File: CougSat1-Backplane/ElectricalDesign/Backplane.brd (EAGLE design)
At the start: 82 x 93 mm, 17 parts, among them J1 CougSat Socket, J10 CougSat Socket, J2 CougSat Socket, J3 CougSat Socket, J4 CougSat Socket, J5 Separation Switch, J6 Separation Switch, J7 CougSat Socket, J8 CougSat Socket, J9 CougSat Socket

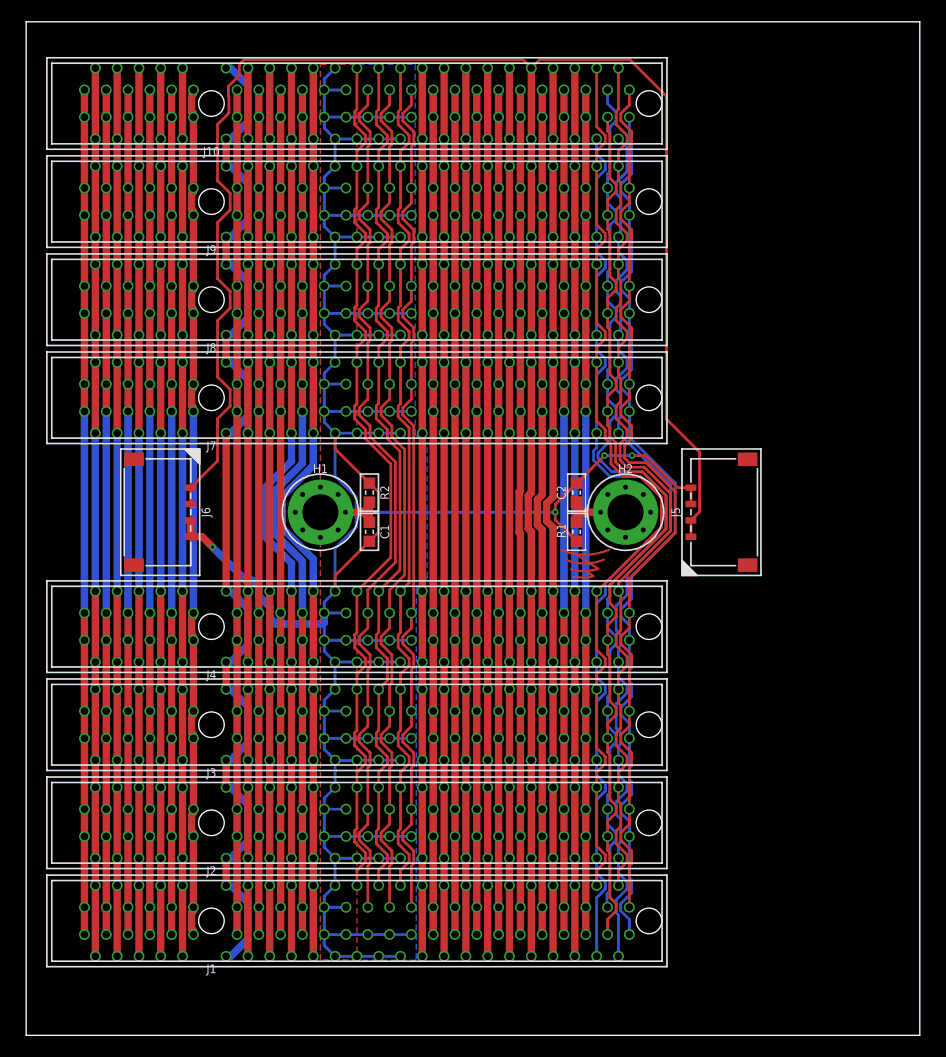
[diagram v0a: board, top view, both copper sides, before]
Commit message: Placed jacks
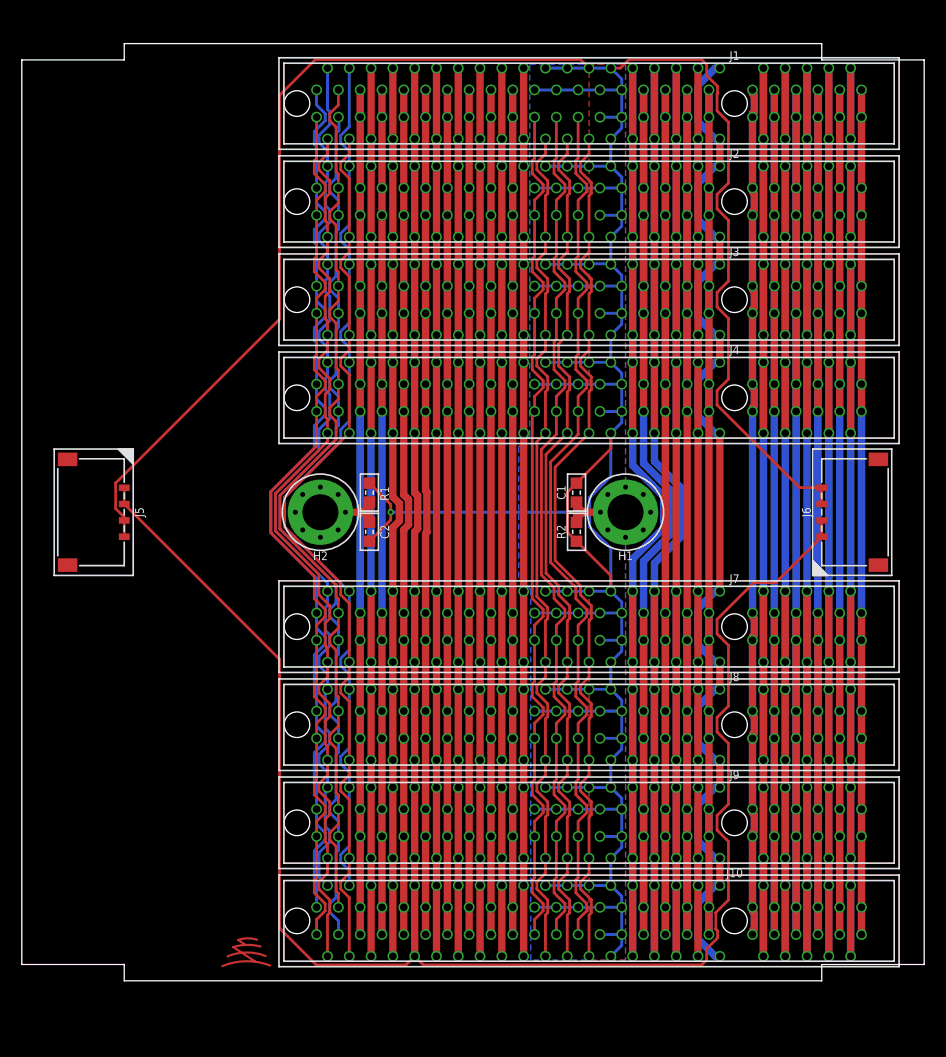
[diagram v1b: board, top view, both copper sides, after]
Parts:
- moved J1 89.0 mm to (24.0, 37.5), turned to 180 degrees
- moved J10 89.0 mm to (24.0, -37.5), turned to 180 degrees
- moved J2 74.5 mm to (24.0, 28.5), turned to 180 degrees
- moved J9 74.5 mm to (24.0, -28.5), turned to 180 degrees
- moved J3 61.8 mm to (24.0, 19.5), turned to 180 degrees
- moved J8 61.8 mm to (24.0, -19.5), turned to 180 degrees
- moved J6 57.9 mm to (32.0, 0.00), turned to 270 degrees
- moved J4 52.4 mm to (24.0, 10.5), turned to 180 degrees
- moved J7 52.4 mm to (24.0, -10.5), turned to 180 degrees
- moved J5 52.0 mm to (-32.0, 0.00), turned to 90 degrees
- moved LOGO1 47.3 mm to (-20.8, -40.4), turned to 90 degrees
- moved H1 28.0 mm to (14.0, 0.00), turned to 180 degrees
- moved H2 28.0 mm to (-14.0, 0.00), turned to 180 degrees
- moved C1 19.3 mm to (9.50, 1.80), turned to 90 degrees
- moved C2 19.3 mm to (-9.50, -1.80), turned to 270 degrees
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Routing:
- net PGND: track 294.2 -> 395.9 mm, vias 4 -> 1
- net PR_BATT-2: track 81.5 -> 148.5 mm
- net PR_3.3V-9: track 81.5 -> 148.5 mm
- net PR_3.3V-7: track 81.5 -> 148.5 mm
- net PR_3.3V-5: track 81.5 -> 148.5 mm
- net PR_3.3V-3: track 81.5 -> 148.5 mm
- net PR_3.3V-1: track 81.5 -> 148.5 mm
- net PR_BATT-4: track 83.6 -> 144.1 mm
- net PR_BATT-6: track 83.9 -> 144.4 mm
- net PR_3.3V-10: track 78.6 -> 138.6 mm
- net PR_BATT-3: track 77.5 -> 136.5 mm
- net PR_BATT-1: track 77.5 -> 136.5 mm
- net PR_3.3V-8: track 77.5 -> 136.5 mm
- net PR_3.3V-6: track 77.5 -> 136.5 mm
- net PR_3.3V-4: track 77.5 -> 136.5 mm
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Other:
- board size 82 x 93 mm -> 82.8 x 86 mm
